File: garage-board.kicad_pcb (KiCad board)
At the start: 2 copper layers, 177.5 x 89 mm, 0 parts

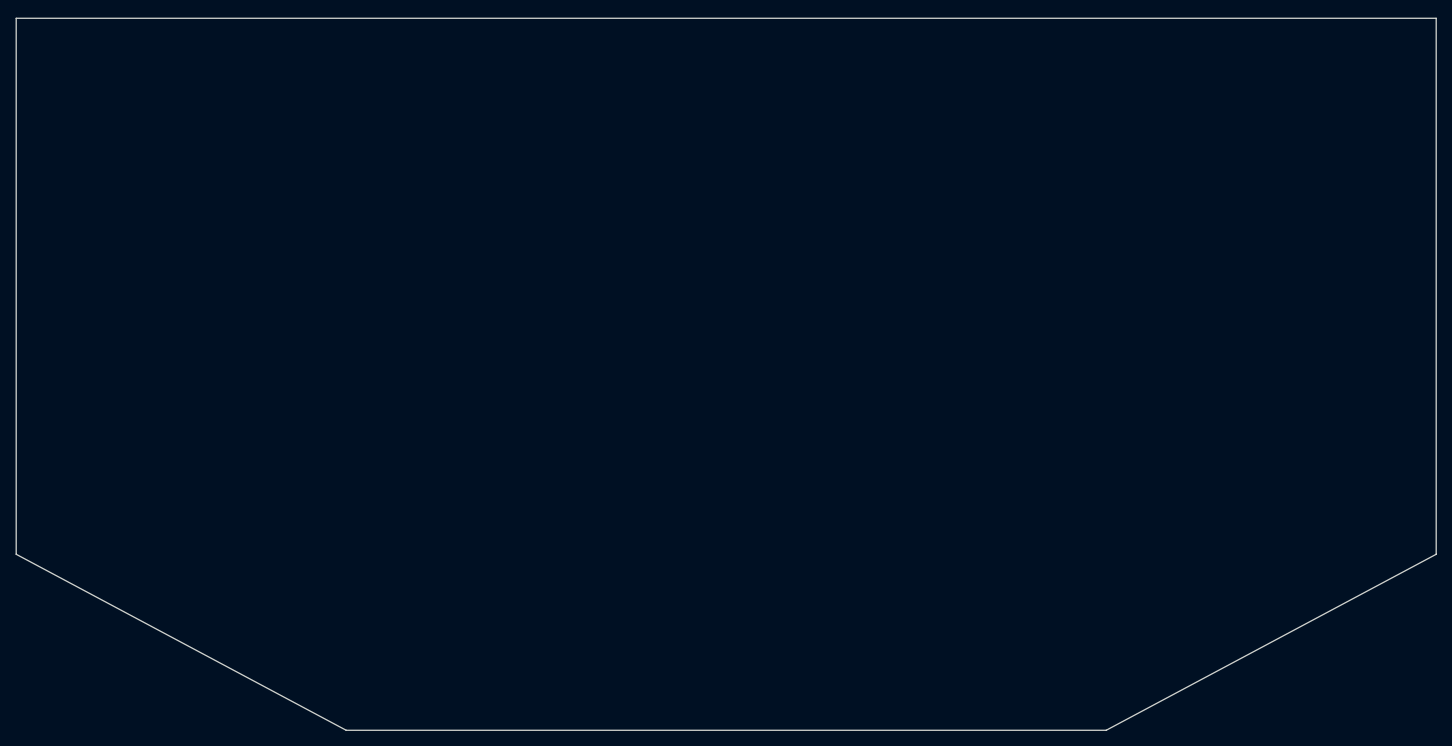
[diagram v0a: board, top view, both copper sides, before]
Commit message: Place components sketch on PCB
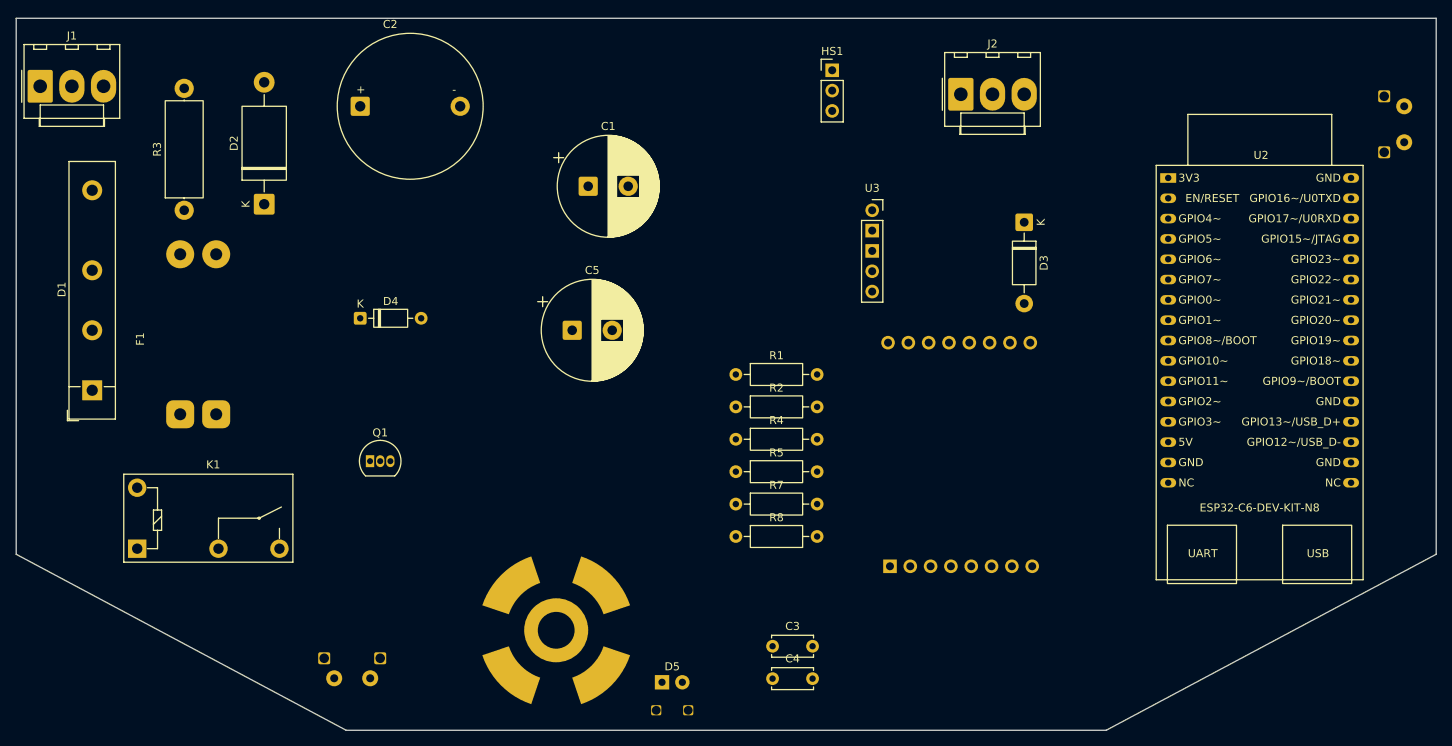
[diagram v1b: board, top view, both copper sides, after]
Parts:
- added C1: 470uF 63V 105C ESR, Capacitor_THT:CP_Radial_D12.5mm_P5.00mm, F.Cu at (121.5, 71.0)
- added C2: 4700uF 63V 105C ESR, garage_board:CP_Radial_D25.0mm_P12.50mm, F.Cu at (93.0, 61.0)
- added C3: 100nF, Capacitor_THT:C_Disc_D5.0mm_W2.5mm_P5.00mm, F.Cu at (144.5, 128.5)
- added C4: 100nF, Capacitor_THT:C_Disc_D5.0mm_W2.5mm_P5.00mm, F.Cu at (144.5, 132.5)
- added C5: 470uF 63V 105C ESR, Capacitor_THT:CP_Radial_D12.5mm_P5.00mm, F.Cu at (119.5, 89.0)
- added D1: B125 C7000-4000, Diode_THT:Diode_Bridge_32.0x5.6x17.0mm_P10.0mm_P7.5mm, F.Cu at (59.5, 96.5)
- added D2: 1.5KE39A, Diode_THT:D_DO-201AE_P15.24mm_Horizontal, F.Cu at (81.0, 73.2)
- added D3: 1N4007, Diode_THT:D_DO-41_SOD81_P10.16mm_Horizontal, F.Cu at (176.0, 75.5)
- added D4: 1N4148, Diode_THT:D_DO-35_SOD27_P7.62mm_Horizontal, F.Cu at (93.0, 87.5)
- added D5: Red, garage_board:LED_D5.0mm_Horizontal, F.Cu at (130.7, 133.0)
- added F1: T6.3A, garage_board:Fuseholder_5x20mm_Lateral_P20.00x5.00mm, F.Cu at (70.5, 99.5)
- added HS1: HAL503, Connector_PinHeader_2.54mm:PinHeader_1x03_P2.54mm_Vertical, F.Cu at (152.0, 56.5)
- added J1: 24VAC, Connector_Molex:Molex_KK-396_A-41791-0003_1x03_P3.96mm_Vertical, F.Cu at (53.0, 58.5)
- added J2: Motor, Connector_Molex:Molex_KK-396_A-41791-0003_1x03_P3.96mm_Vertical, F.Cu at (168.1, 59.5)
- added K1: G5Q-1A, Relay_THT:Relay_SPST_Omron-G5Q-1A, F.Cu at (65.1, 116.3)
- added LA1: Lamp, garage_board:lamp, F.Cu at (117.5, 126.5)
- added Q1: BC547, Package_TO_SOT_THT:TO-92_Inline, F.Cu at (94.2, 105.4)
- added R1: 4.7k, Resistor_THT:R_Axial_DIN0207_L6.3mm_D2.5mm_P10.16mm_Horizontal, F.Cu at (140.0, 94.5)
- added R2: 10k, Resistor_THT:R_Axial_DIN0207_L6.3mm_D2.5mm_P10.16mm_Horizontal, F.Cu at (140.0, 98.6)
- added R3: 10k (0.5W), Resistor_THT:R_Axial_DIN0414_L11.9mm_D4.5mm_P15.24mm_Horizontal, F.Cu at (71.0, 74.0)
- added R4: 4.7k, Resistor_THT:R_Axial_DIN0207_L6.3mm_D2.5mm_P10.16mm_Horizontal, F.Cu at (140.0, 102.6)
- added R5: 1k, Resistor_THT:R_Axial_DIN0207_L6.3mm_D2.5mm_P10.16mm_Horizontal, F.Cu at (140.0, 106.7)
- added R7: 4.7k, Resistor_THT:R_Axial_DIN0207_L6.3mm_D2.5mm_P10.16mm_Horizontal, F.Cu at (140.0, 110.7)
- added R8: 680, Resistor_THT:R_Axial_DIN0207_L6.3mm_D2.5mm_P10.16mm_Horizontal, F.Cu at (140.0, 114.8)
- added SW2: SW_Push, garage_board:Switch, F.Cu at (223.5, 65.5)
- added SW3: SW_Push, garage_board:Switch, F.Cu at (89.8, 132.5)
- added U1: Pololu-2993, garage_board:Pololu Motor Driver 2993, F.Cu at (159.2, 118.5)
- added U2: ESP32-C6-DEV-KIT-N8, PCM_Espressif:ESP32-C6-DevKitC-1, F.Cu at (194.0, 70.0)
- added U3: Pololu-4892, garage_board:Pololu 4892, F.Cu at (157.0, 74.0)
